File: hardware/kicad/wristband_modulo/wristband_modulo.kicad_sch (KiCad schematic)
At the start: 11 parts, among them J1 Battery_Negative_Contact, U1 E73-2G4M04S-52810

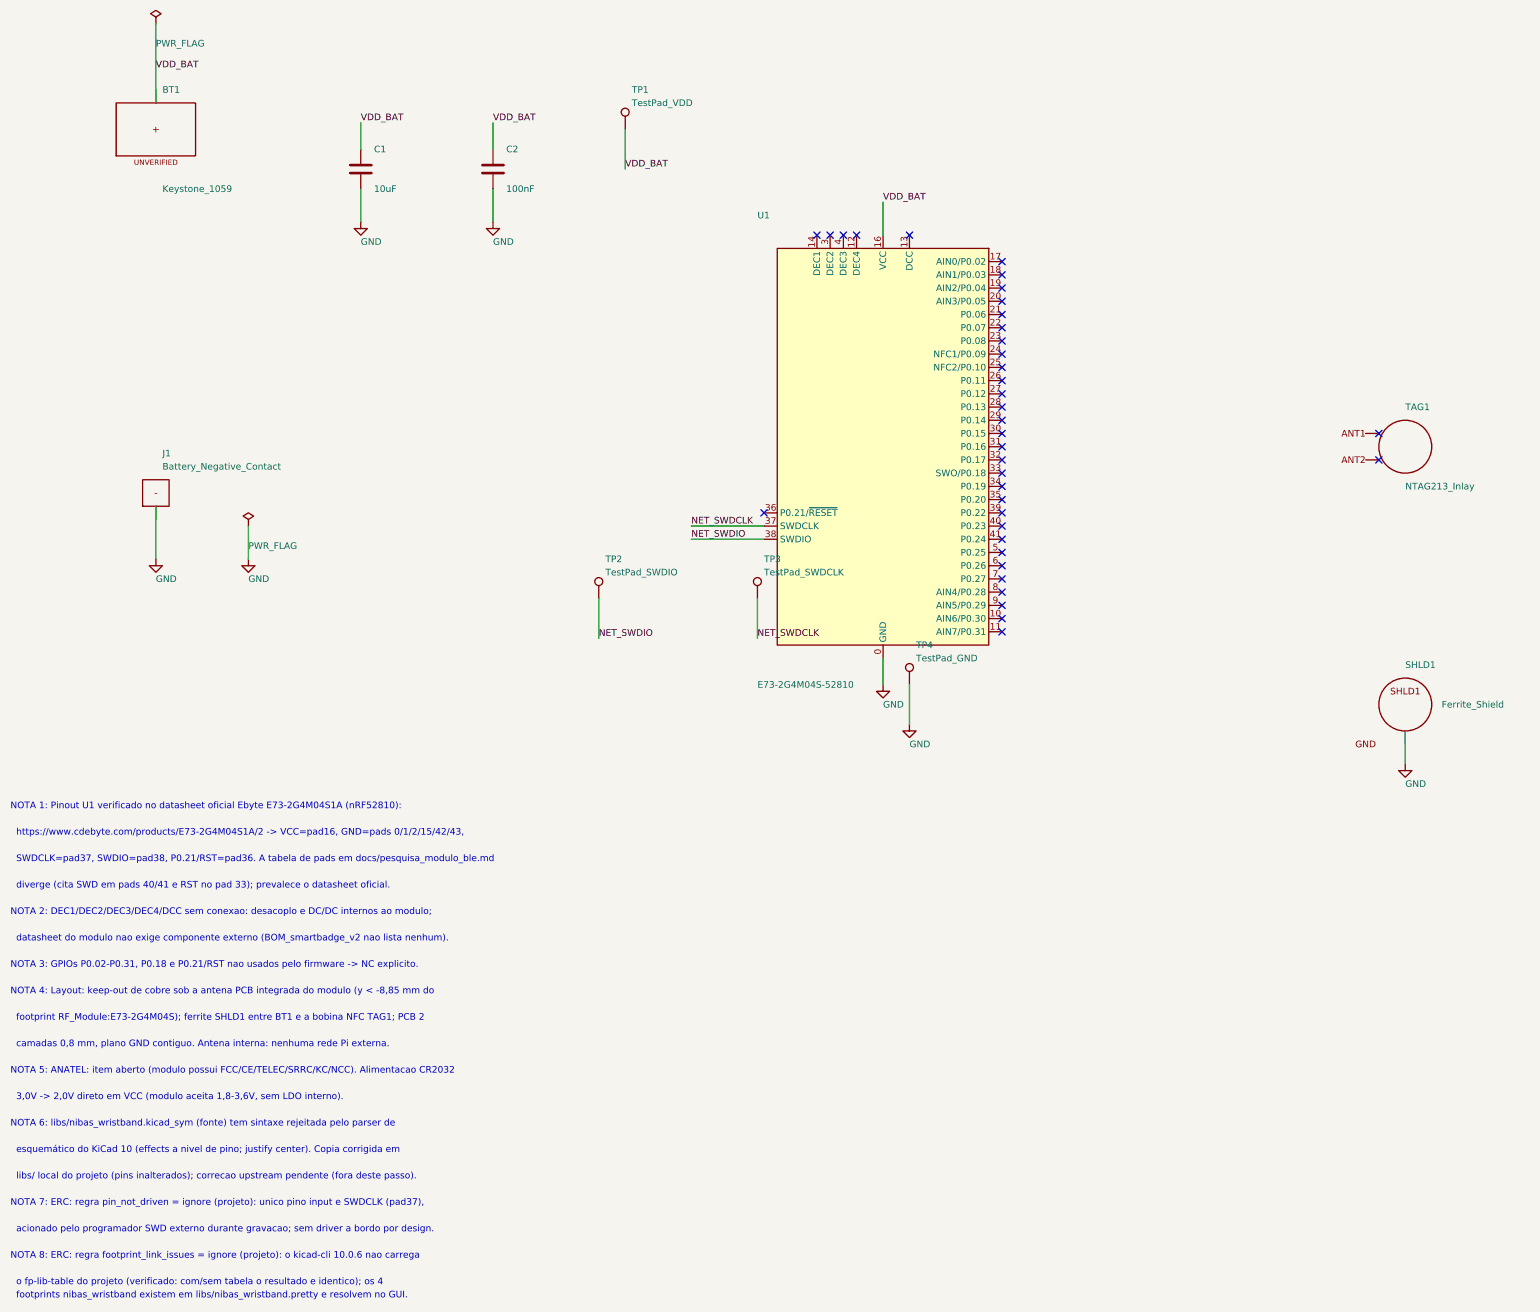
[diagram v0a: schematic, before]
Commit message: Layouts finish, BM832A migration, fab package, quote, docs and status report
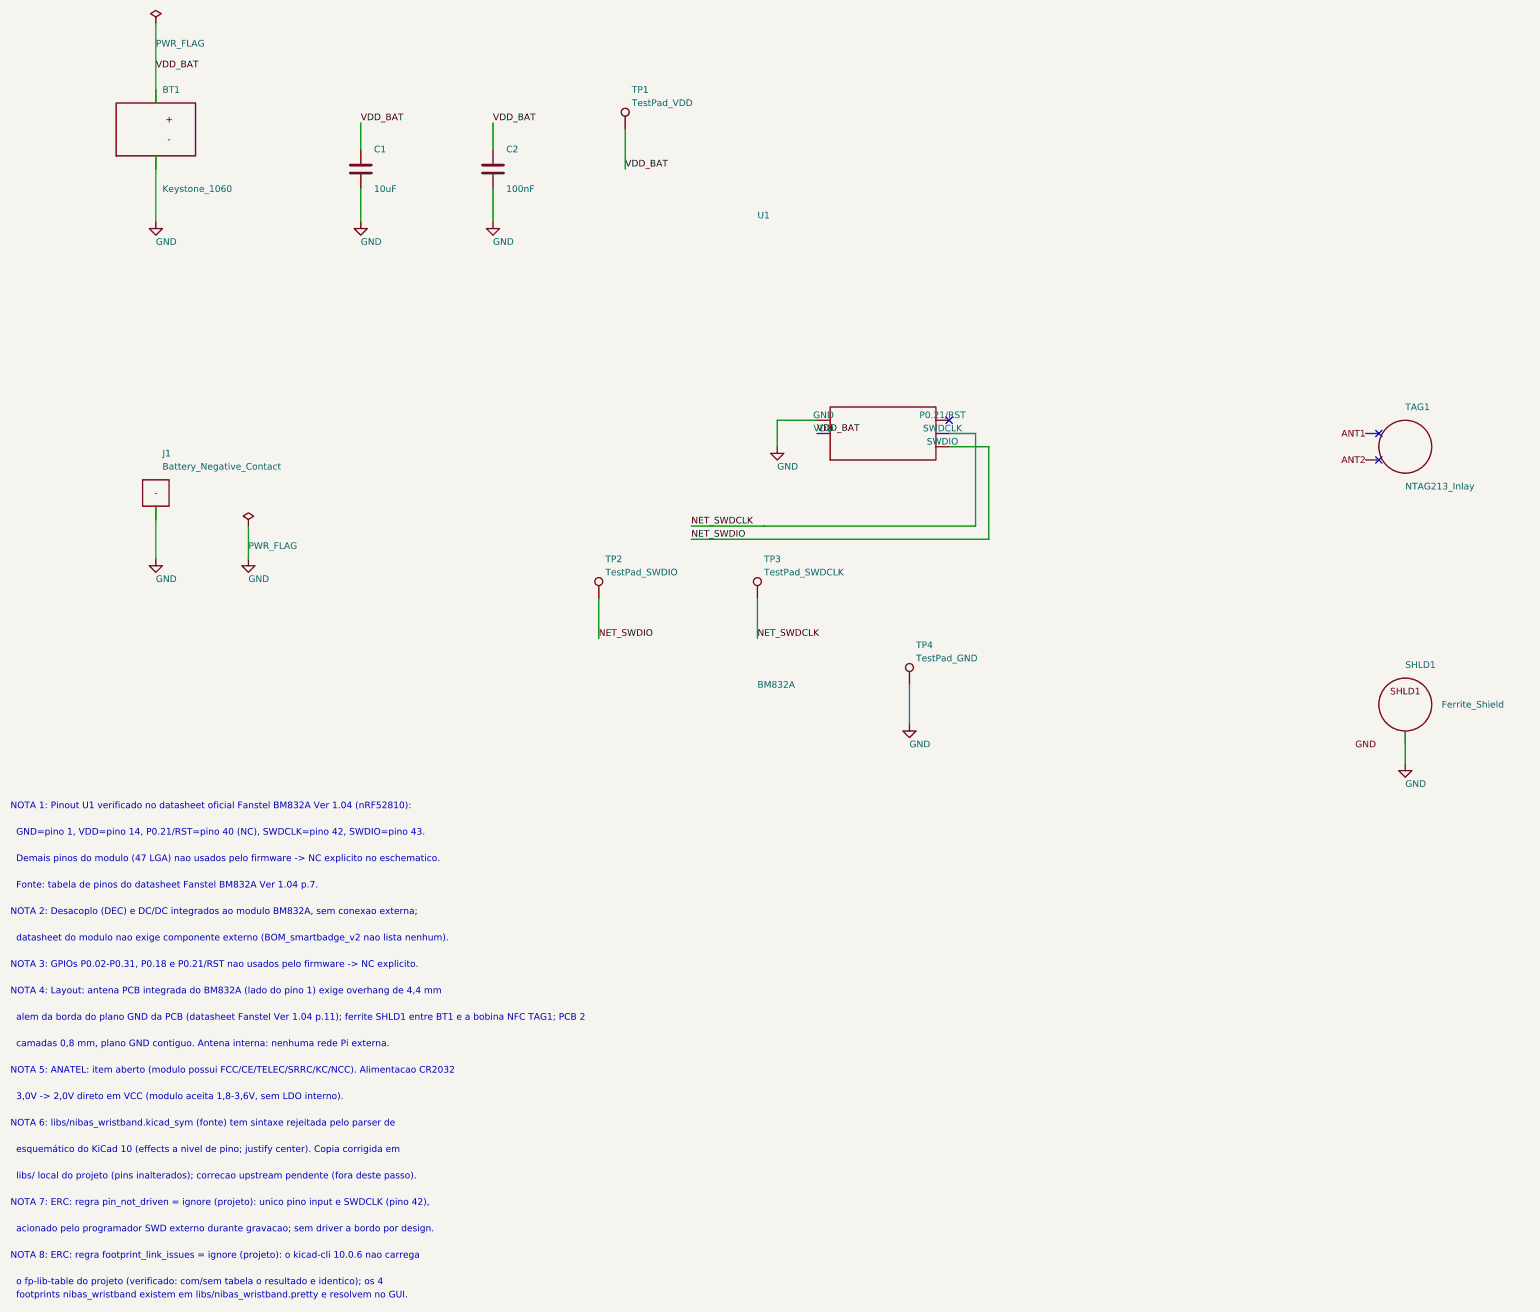
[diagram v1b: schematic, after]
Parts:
- BT1: value Keystone_1059 -> Keystone_1060; footprint nibas_wristband:Keystone_1059_CR2032_SMT -> nibas_wristband:Keystone_1060_CR2032_SMT; symbol nibas_wristband:Keystone_1059 -> nibas_wristband:Keystone_1060
- U1: value E73-2G4M04S-52810 -> BM832A; footprint RF_Module:E73-2G4M04S -> nibas_wristband:BM832A; symbol RF_Module:E73-2G4M04S-52810 -> nibas_wristband:BM832A
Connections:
- net GND: now also BT1.2 (GND); no longer U1.0 (GND), U1.15 (GND), U1.2 (GND), U1.42 (GND), U1.43 (GND)
- net NET_SWDCLK: now also U1.42 (SWDCLK); no longer U1.37 (SWDCLK)
- net NET_SWDIO: now also U1.43 (SWDIO); no longer U1.38 (SWDIO)
- net VDD_BAT: now also U1.14 (VDD); no longer U1.16 (VCC)
- no-connect marks 37 -> 3
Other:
- note added: "Demais pinos do modulo (47 LGA) nao usados pelo firmware -> NC explicito no eschematico."
- note added: "Fonte: tabela de pinos do datasheet Fanstel BM832A Ver 1.04 p.7."
- note added: "GND=pino 1, VDD=pino 14, P0.21/RST=pino 40 (NC), SWDCLK=pino 42, SWDIO=pino 43."
- note added: "NOTA 1: Pinout U1 verificado no datasheet oficial Fanstel BM832A Ver 1.04 (nRF52810):"
- note added: "NOTA 2: Desacoplo (DEC) e DC/DC integrados ao modulo BM832A, sem conexao externa;"
- note added: "NOTA 4: Layout: antena PCB integrada do BM832A (lado do pino 1) exige overhang de 4,4 mm"
- note added: "NOTA 7: ERC: regra pin_not_driven = ignore (projeto): unico pino input e SWDCLK (pino 42),"
- note added: "alem da borda do plano GND da PCB (datasheet Fanstel Ver 1.04 p.11); ferrite SHLD1 entre BT1 e a bobina NFC TAG1; PCB 2"
- note removed: "NOTA 1: Pinout U1 verificado no datasheet oficial Ebyte E73-2G4M04S1A (nRF52810):"
- note removed: "NOTA 2: DEC1/DEC2/DEC3/DEC4/DCC sem conexao: desacoplo e DC/DC internos ao modulo;"
- note removed: "NOTA 4: Layout: keep-out de cobre sob a antena PCB integrada do modulo (y < -8,85 mm do"
- note removed: "NOTA 7: ERC: regra pin_not_driven = ignore (projeto): unico pino input e SWDCLK (pad37),"
- note removed: "SWDCLK=pad37, SWDIO=pad38, P0.21/RST=pad36. A tabela de pads em docs/pesquisa_modulo_ble.md"
- note removed: "diverge (cita SWD em pads 40/41 e RST no pad 33); prevalece o datasheet oficial."
- note removed: "footprint RF_Module:E73-2G4M04S); ferrite SHLD1 entre BT1 e a bobina NFC TAG1; PCB 2"
- note removed: "https://www.cdebyte.com/products/E73-2G4M04S1A/2 -> VCC=pad16, GND=pads 0/1/2/15/42/43,"
